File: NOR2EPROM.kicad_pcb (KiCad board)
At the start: 2 copper layers, 7 parts, among them U1 SN74LVC245APW, U2 SN74LVC245APW, U3 MX29LV320, U4 27C322, U5 SN74LVC245APW, U6 SN74LVC245APW, U7 SN74LVC245APW

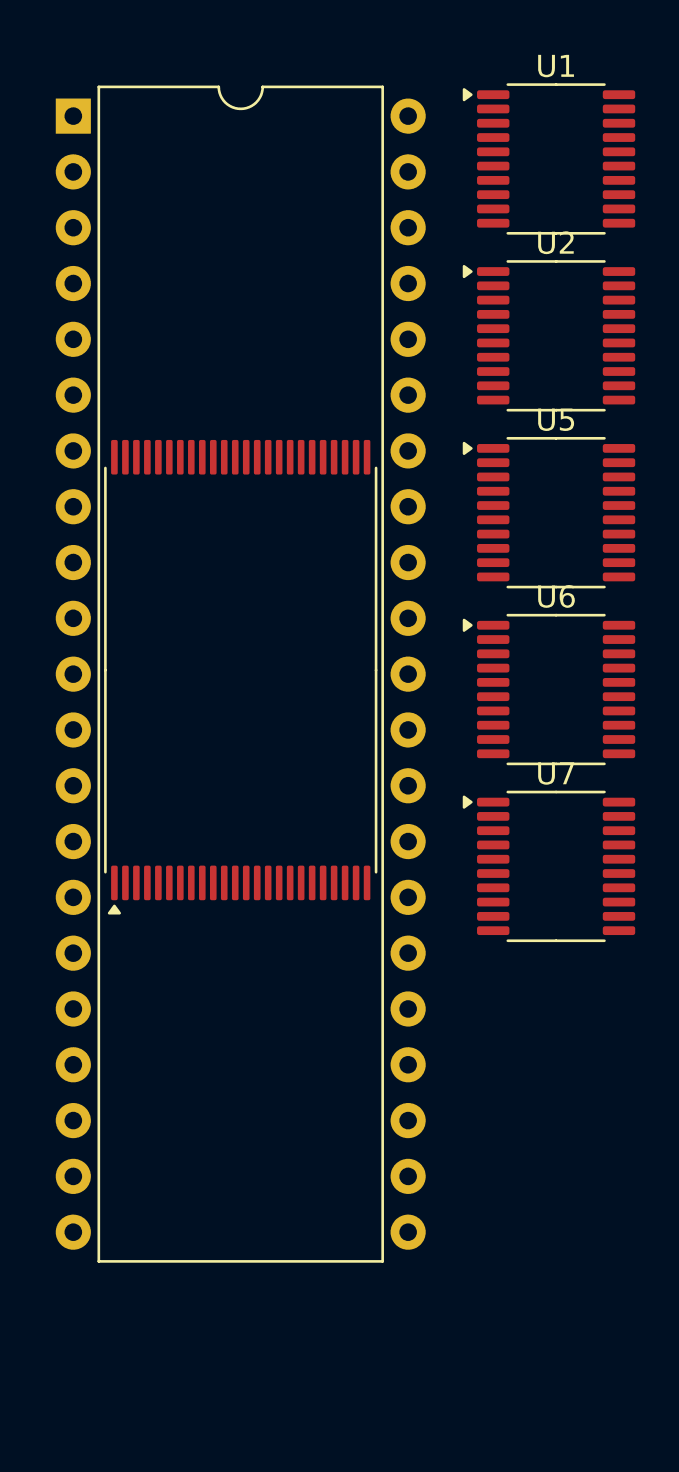
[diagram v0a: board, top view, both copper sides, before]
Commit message: add output cap, position components before routing
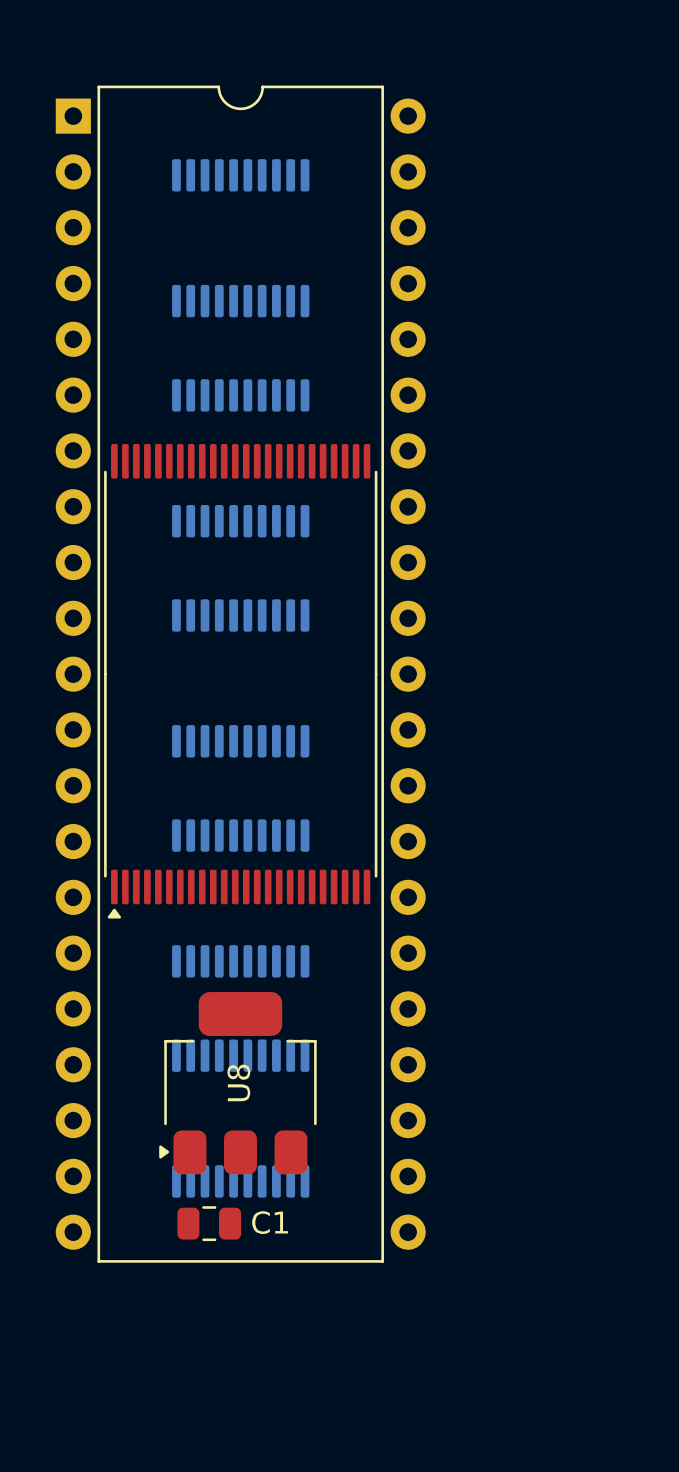
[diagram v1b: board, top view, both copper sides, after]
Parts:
- added C1: 10uF, Capacitor_SMD:C_0805_2012Metric, F.Cu at (114.0, 112.7)
- added U8: LD1117S33TR_SOT223, Package_TO_SOT_SMD:SOT-223-3_TabPin2, F.Cu at (115.5, 106.3)
- U1, U2, U5: value SN74LVC245APW -> SN74LVC245; moved to B.Cu
- U6, U7: value SN74LVC245APW -> SN74HCT245; moved to B.Cu
- moved U7 18.4 mm to (115.5, 107.9), turned to 90 degrees
- moved U6 17.2 mm to (115.5, 97.9), turned to 90 degrees
- moved U5 16.2 mm to (115.5, 87.9), turned to 90 degrees
- moved U2 15.4 mm to (115.5, 77.9), turned to 90 degrees
- moved U1 14.8 mm to (115.5, 67.8), turned to 90 degrees
- moved U3 0.19 mm to (115.5, 87.7)
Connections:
- U1 pad 1: unconnected-(U1-DIR-Pad1) -> GND
- U1 pad 11: NOR_A7 -> EPROM_A7
- U1 pad 12: NOR_A6 -> EPROM_A6
- U1 pad 13: NOR_A5 -> EPROM_A5
- U1 pad 14: NOR_A4 -> EPROM_A4
- U1 pad 15: NOR_A3 -> EPROM_A3
- U1 pad 16: NOR_A2 -> EPROM_A2
- U1 pad 17: NOR_A1 -> EPROM_A1
- U1 pad 18: NOR_A0 -> EPROM_A0
- U1 pad 19: unconnected-(U1-~{OE}-Pad19) -> GND
- U1 pad 2: EPROM_A0 -> NOR_A0
- U1 pad 20: unconnected-(U1-VCC-Pad20) -> +3.3V
- U1 pad 3: EPROM_A1 -> NOR_A1
- U1 pad 4: EPROM_A2 -> NOR_A2
- U1 pad 5: EPROM_A3 -> NOR_A3
- U1 pad 6: EPROM_A4 -> NOR_A4
- U1 pad 7: EPROM_A5 -> NOR_A5
- U1 pad 8: EPROM_A6 -> NOR_A6
- U1 pad 9: EPROM_A7 -> NOR_A7
- U2 pad 1: unconnected-(U2-DIR-Pad1) -> GND
- U2 pad 11: NOR_A15 -> EPROM_A15
- U2 pad 12: NOR_A14 -> EPROM_A14
- U2 pad 13: NOR_A13 -> EPROM_A13
- U2 pad 14: NOR_A12 -> EPROM_A12
- U2 pad 15: NOR_A11 -> EPROM_A11
- U2 pad 16: NOR_A10 -> EPROM_A10
- U2 pad 17: NOR_A9 -> EPROM_A9
- U2 pad 18: NOR_A8 -> EPROM_A8
- U2 pad 19: unconnected-(U2-~{OE}-Pad19) -> GND
- U2 pad 2: EPROM_A8 -> NOR_A8
- U2 pad 20: unconnected-(U2-VCC-Pad20) -> +3.3V
- U2 pad 3: EPROM_A9 -> NOR_A9
- U2 pad 4: EPROM_A10 -> NOR_A10
- U2 pad 5: EPROM_A11 -> NOR_A11
- U2 pad 6: EPROM_A12 -> NOR_A12
- U2 pad 7: EPROM_A13 -> NOR_A13
- U2 pad 8: EPROM_A14 -> NOR_A14
- U2 pad 9: EPROM_A15 -> NOR_A15
- U3 pad 26: unconnected-(U3-~{CE}-Pad26) -> CHIP_ENABLE
- U3 pad 27: unconnected-(U3-GND-Pad27) -> GND
- U3 pad 28: unconnected-(U3-~{OE}-Pad28) -> OUTPUT_ENABLE
- U3 pad 37: unconnected-(U3-VCC-Pad37) -> +3.3V
- U3 pad 46: unconnected-(U3-GND-Pad46) -> GND
- U3 pad 47: unconnected-(U3-~{BYTE}-Pad47) -> +3.3V
- U4 pad 11: unconnected-(U4-~{E}-Pad11) -> CHIP_ENABLE
- U4 pad 12: unconnected-(U4-Vss-Pad12) -> GND
- U4 pad 13: unconnected-(U4-~{G}Vpp-Pad13) -> OUTPUT_ENABLE
- U4 pad 22: unconnected-(U4-Vcc-Pad22) -> +5V
- U4 pad 31: unconnected-(U4-Vss-Pad31) -> GND
- U5 pad 1: unconnected-(U5-DIR-Pad1) -> GND
- U5 pad 14: NOR_A20 -> EPROM_A20
- U5 pad 15: NOR_A19 -> EPROM_A19
- U5 pad 16: NOR_A18 -> EPROM_A18
- U5 pad 17: NOR_A17 -> EPROM_A17
- U5 pad 18: NOR_A16 -> EPROM_A16
- U5 pad 19: unconnected-(U5-~{OE}-Pad19) -> GND
- U5 pad 2: EPROM_A16 -> NOR_A16
- U5 pad 20: unconnected-(U5-VCC-Pad20) -> +3.3V
- U5 pad 3: EPROM_A17 -> NOR_A17
- U5 pad 4: EPROM_A18 -> NOR_A18
- U5 pad 5: EPROM_A19 -> NOR_A19
- U5 pad 6: EPROM_A20 -> NOR_A20
- U6 pad 1: unconnected-(U6-DIR-Pad1) -> GND
- U6 pad 19: unconnected-(U6-~{OE}-Pad19) -> GND
- U6 pad 20: unconnected-(U6-VCC-Pad20) -> +5V
- U7 pad 1: unconnected-(U7-DIR-Pad1) -> GND
- U7 pad 19: unconnected-(U7-~{OE}-Pad19) -> GND
- U7 pad 20: unconnected-(U7-VCC-Pad20) -> +5V

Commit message: routing checkpoint
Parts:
- U2, U5, U6: moved to F.Cu
- moved U2 25.8 mm to (112.4, 103.5), turned to -90 degrees
- moved U6 25.6 mm to (115.6, 72.3), turned to -90 degrees
- moved U1 24.9 mm to (118.1, 92.6)
- moved U7 24.1 mm to (115.5, 83.8)
- moved U5 23.2 mm to (118.1, 110.9), turned to 0 degrees
- moved U8 11.9 mm to (117.2, 118.1), turned to 0 degrees
- moved U4 7.38 mm to (107.8, 69.7)
- moved C1 4.80 mm to (111.8, 116.9), turned to 90 degrees
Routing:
- net EPROM_Q6: track 0.00 -> 79.5 mm, vias 0 -> 3
- net EPROM_Q4: track 0.00 -> 73.9 mm, vias 0 -> 3
- net EPROM_Q5: track 0.00 -> 73.8 mm, vias 0 -> 3
- net EPROM_Q3: track 0.00 -> 53.9 mm, vias 0 -> 2
- net EPROM_A18: track 0.00 -> 49.5 mm, vias 0 -> 1
- net EPROM_Q2: track 0.00 -> 48.5 mm, vias 0 -> 3
- net EPROM_A17: track 0.00 -> 47.7 mm, vias 0 -> 2
- net EPROM_Q7: track 0.00 -> 47.1 mm, vias 0 -> 2
- net EPROM_Q1: track 0.00 -> 45.1 mm, vias 0 -> 1
- net EPROM_Q11: track 0.00 -> 41.6 mm, vias 0 -> 1
- net EPROM_Q10: track 0.00 -> 40.7 mm, vias 0 -> 2
- net EPROM_Q0: track 0.00 -> 39.8 mm, vias 0 -> 1
- net EPROM_Q9: track 0.00 -> 35.7 mm, vias 0 -> 2
- net NOR_A16: track 0.00 -> 33.9 mm, vias 0 -> 2
- net OUTPUT_ENABLE: track 0.00 -> 32.8 mm, vias 0 -> 1
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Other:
- copper layers 2 -> 4

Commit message: finished routing
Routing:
- net +5V: track 6.35 -> 77.3 mm, vias 1 -> 3
- net +3.3V: track 7.81 -> 78.3 mm, vias 2 -> 6
- net GND: track 0.00 -> 69.8 mm, vias 0 -> 10
- net EPROM_A19: track 0.00 -> 65.4 mm, vias 0 -> 2
- net EPROM_Q15: track 0.00 -> 57.0 mm, vias 0 -> 1
- net EPROM_Q14: track 0.00 -> 51.6 mm, vias 0 -> 1
- net EPROM_A12: track 0.00 -> 50.4 mm, vias 0 -> 2
- net EPROM_A10: track 0.00 -> 47.0 mm, vias 0 -> 2
- net EPROM_A11: track 0.00 -> 46.9 mm, vias 0 -> 2
- net EPROM_A8: track 0.00 -> 46.7 mm, vias 0 -> 2
- net EPROM_Q13: track 0.00 -> 45.6 mm, vias 0 -> 1
- net EPROM_Q12: track 0.00 -> 42.9 mm, vias 0 -> 1
- net EPROM_A13: track 0.00 -> 42.2 mm, vias 0 -> 2
- net EPROM_A9: track 0.00 -> 41.9 mm, vias 0 -> 2
- net EPROM_A14: track 0.00 -> 38.8 mm, vias 0 -> 2
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- added copper zone on In2.Cu, net GND

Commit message: fix drc errors
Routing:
- net GND: track 69.8 -> 113.0 mm, vias 10 -> 11
- net +3.3V: track 78.3 -> 81.8 mm
- net EPROM_A9: track 41.9 -> 43.8 mm
- net EPROM_A8: track 46.7 -> 48.1 mm
- net EPROM_A12: track 50.4 -> 49.0 mm
- net EPROM_A4: track 19.2 -> 18.0 mm
- net EPROM_A7: track 20.9 -> 19.9 mm
- net EPROM_A19: track 65.4 -> 66.3 mm
- net EPROM_Q10: track 41.3 -> 40.5 mm
- net NOR_A7: track 20.5 -> 19.8 mm
- net EPROM_A10: track 47.0 -> 46.5 mm
- net +5V: track 77.3 -> 76.8 mm
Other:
- board outline added: 17.8 x 54 mm

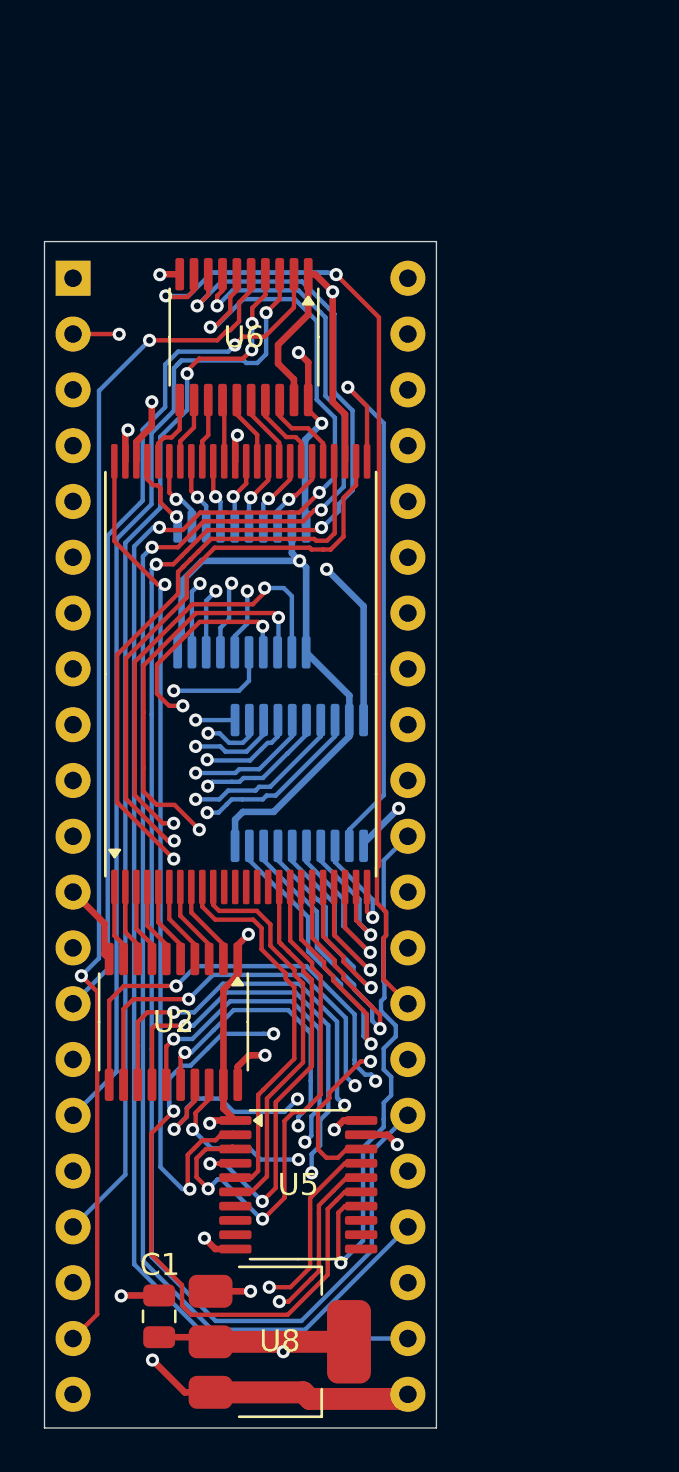
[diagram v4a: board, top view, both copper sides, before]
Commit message: level shift OE and CE lines
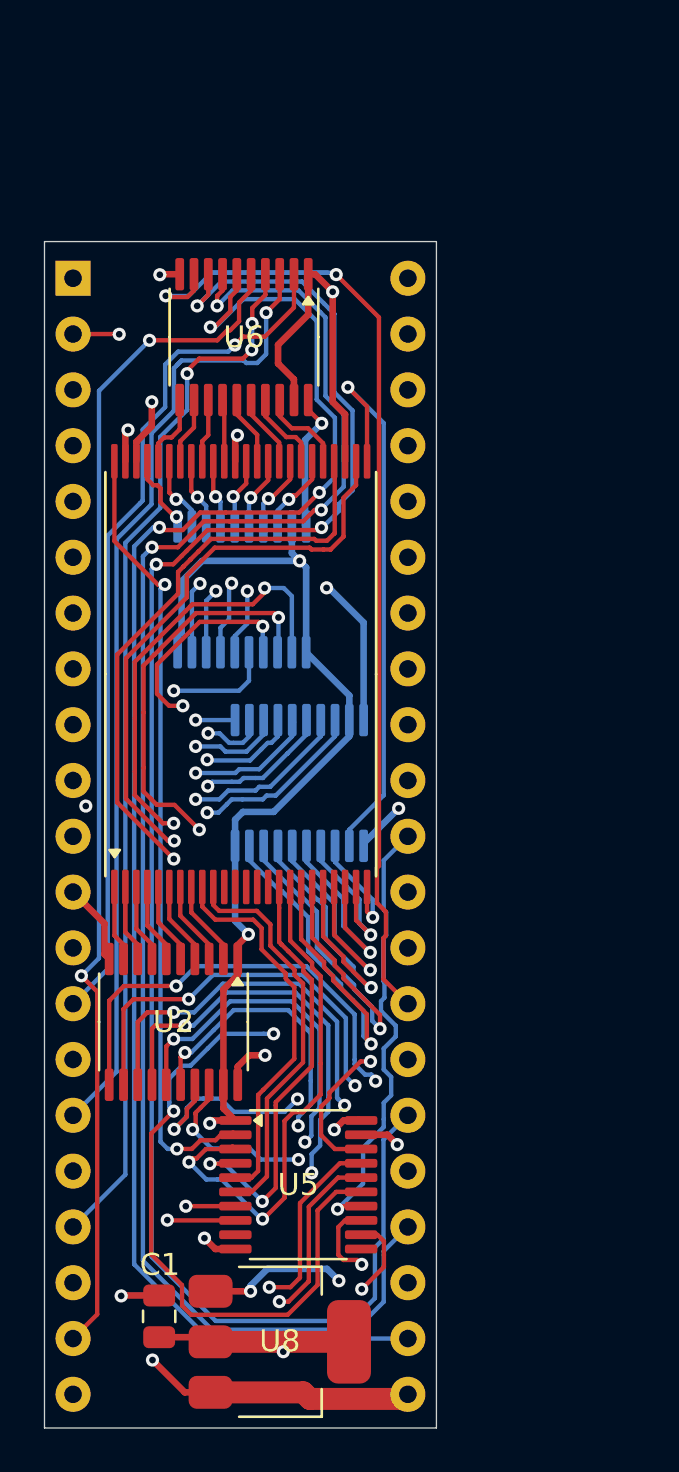
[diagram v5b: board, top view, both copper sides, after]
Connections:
- U3 pad 26: CHIP_ENABLE -> NOR_CE
- U3 pad 28: OUTPUT_ENABLE -> NOR_OE
- U4 pad 11: CHIP_ENABLE -> EPROM_CE
- U4 pad 13: OUTPUT_ENABLE -> EPROM_OE
- U5 pad 12: unconnected-(U5-B7-Pad12) -> EPROM_CE
- U5 pad 13: unconnected-(U5-B6-Pad13) -> EPROM_OE
- U5 pad 7: unconnected-(U5-A6-Pad7) -> NOR_OE
- U5 pad 8: unconnected-(U5-A7-Pad8) -> NOR_CE
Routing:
- net GND: track 113.0 -> 176.2 mm, vias 11 -> 13
- net NOR_CE: track 0.00 -> 47.5 mm, vias 0 -> 2
- net NOR_OE: track 0.00 -> 45.9 mm, vias 0 -> 2
- net EPROM_CE: track 0.00 -> 44.8 mm, vias 0 -> 1
- net EPROM_OE: track 0.00 -> 41.8 mm, vias 0 -> 1
- net OUTPUT_ENABLE: track 32.8 -> 0.00 mm, vias 1 -> 0
- net CHIP_ENABLE: track 30.7 -> 0.00 mm, vias 1 -> 0
- net +5V: track 76.8 -> 68.7 mm, vias 3 -> 2
- net EPROM_A20: track 25.1 -> 20.4 mm
- net +3.3V: track 81.8 -> 85.2 mm
- net NOR_A16: track 39.4 -> 36.2 mm
- net EPROM_Q5: track 73.2 -> 74.5 mm
- net EPROM_Q6: track 78.9 -> 80.2 mm
- net EPROM_A16: track 21.5 -> 20.6 mm
